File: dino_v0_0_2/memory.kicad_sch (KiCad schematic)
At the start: 15 parts, among them U19 74LS245, U21 74LS245, U24 AT28C256, U26 MCM60256AP, U51 7400, U74 74LS00, U75 74LS32

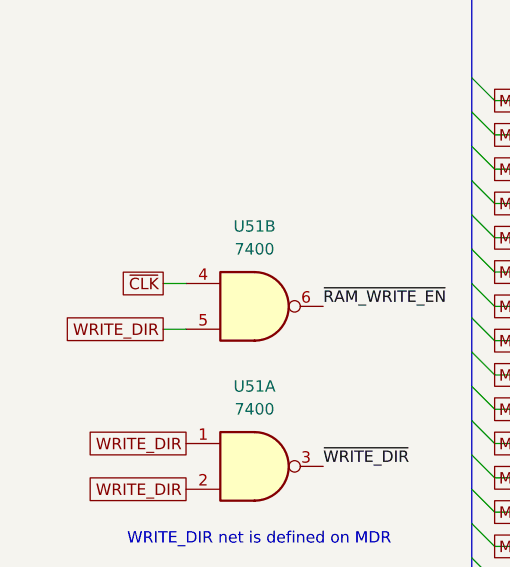
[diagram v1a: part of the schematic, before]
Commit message: fix(copper): gate the RAM write strobe off in T-state 0; RAM-fetch halt closed
A RET fetched from RAM latched 0xFF. Scope work on 2026-09-29 found the
cause: the FETCH row's transparent IR moves the microcode EEPROM address
during CLK-low, the DST decoder (U30.7, code 111 = ~RAM_LOAD) runts for
14-16 ns on some opcode transitions, and NAND(WRITE_DIR, ~CLK) is open
then. The RAM got a 14 ns ~WE at PC's address; the cell survived, the
chip's read output did not, and IR latched 0xFF. From ROM the same runt
is harmless (M15 = 0). The same runt reached ~IO_WR and wrote 0x00 into
[MAR] at every RESET.

Fix: ~RAM_WRITE_EN = NAND(WRITE_DIR, WR_GATE), WR_GATE = NOR(CLK, ~TO0)
on U62 g4, with U56 3->4 inverting TO0 (U7.15). Drawn on control_word
(U62 g4), root (U56 sec 2) and memory (U51.4 label); ERC 0; six pins
beeped good against the drawing.

Witnesses: retlda 40/40 return (was 7/8 halting), no ~WE pulse under
59 ns in 10 runs on a pulse trigger, step2/retmvi/retcrlf/callret/
retinr/retldam/rethlsp 5/5 each, bigxfer returns, a planted byte at
0x8200 survives halt + RESET, and asm/ram/life.asm (Rule 30) runs to the
wall for the first time.

Docs: CLAUDE.md rewritten present-tense (facts only); every retraction
moved to .git/sdd/MISTAKES_MISSTEPS.md. test_ramret.py's table is marked
as the pre-gate record. RAM image headers stamped with the post-gate
result. dino_sheet_contracts.md regenerated by kicad_contracts.py.

Co-Authored-By: Claude Fable 5.1 <noreply@anthropic.com>
Claude-Session: https://claude.ai/code/session_01JGxSS4MVUcaZdKZGtKroSg
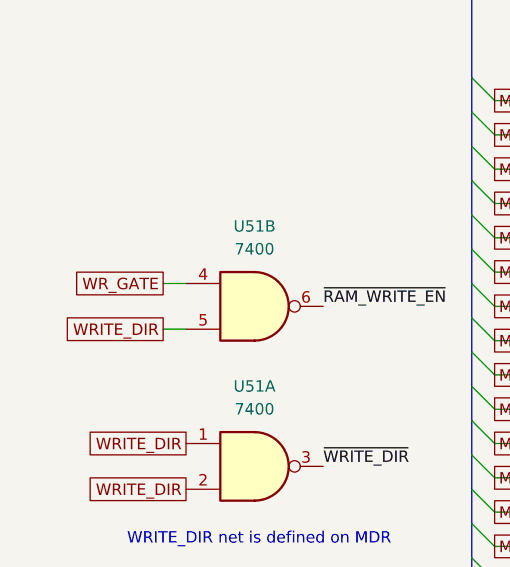
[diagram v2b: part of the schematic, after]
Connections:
- net ~{CLK} renamed WR_GATE
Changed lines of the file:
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@@
 		)
 	)
-	(global_label "~{CLK}"
+	(global_label "WR_GATE"
 		(shape passive)
 		(at 26.67 63.5 180)

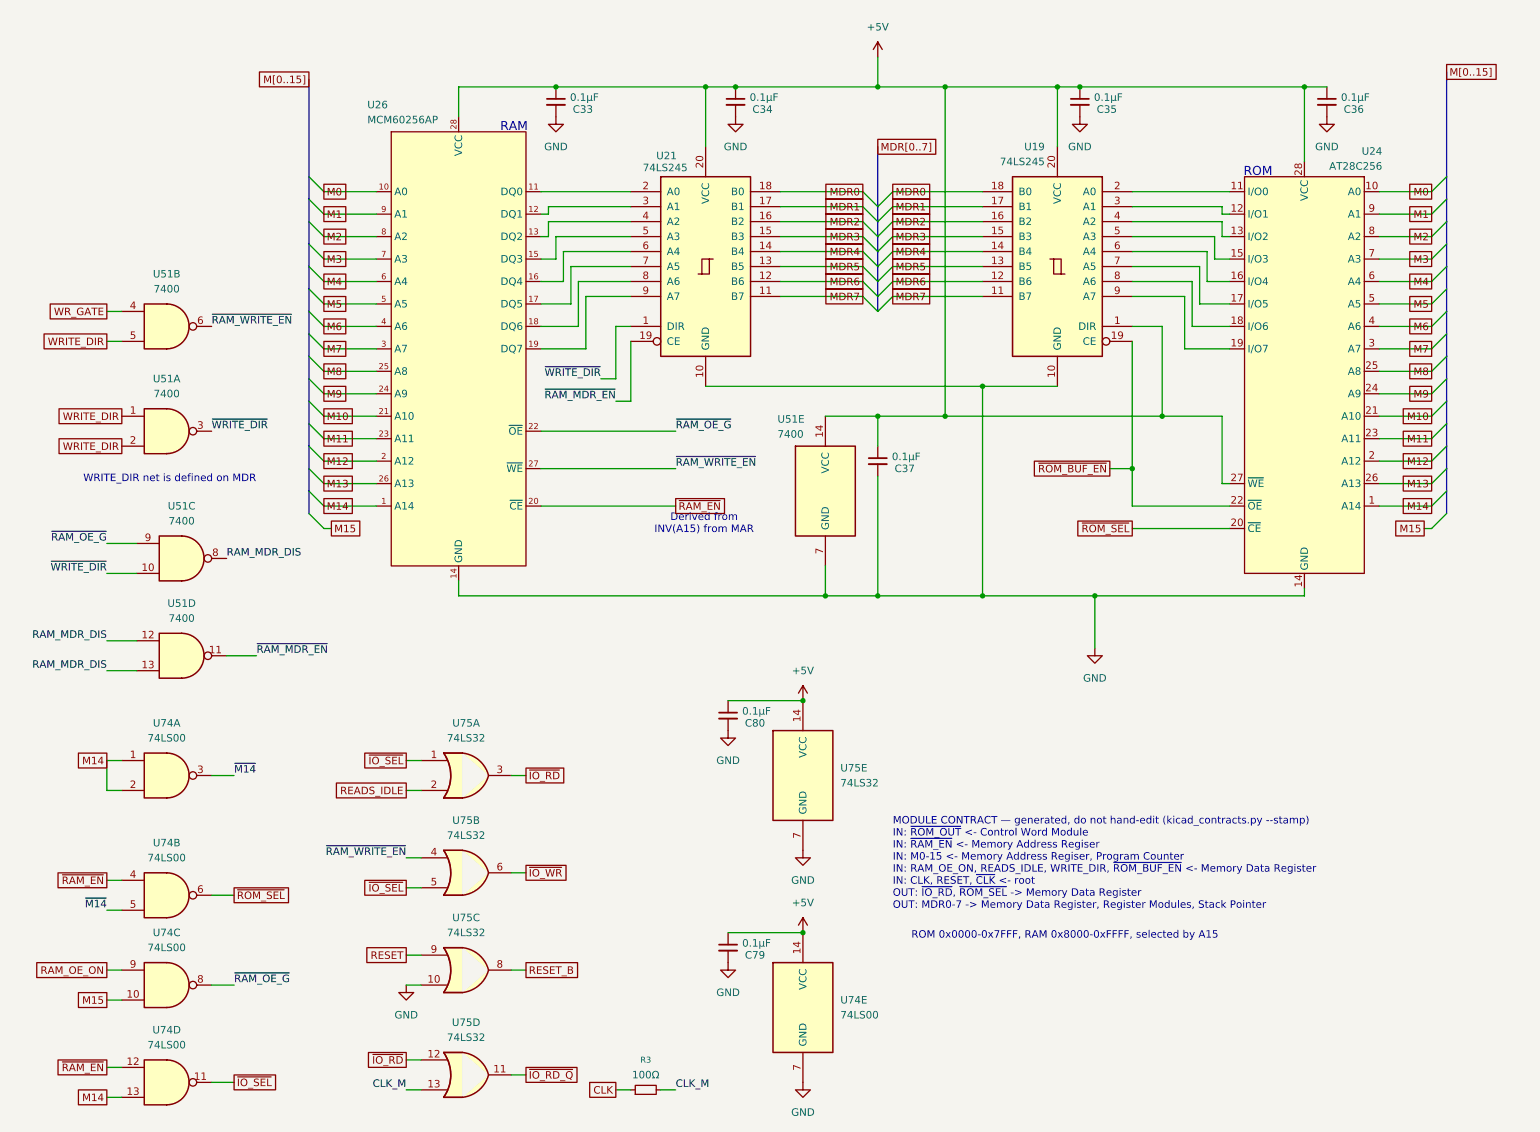
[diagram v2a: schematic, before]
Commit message: feat(int): draw the interrupt block; sheet cleanup pass
New sheet dino_v0_0_2/interrupt.kicad_sch (page 15): U80-U87, R28 4.7k
pull-up on ~{IRQ}, R29 100R on the block's CLK branch, C83-C90. Every
pin per PHASE_INT SECTION 3, checked against the plan with kicad_netlist
and kicad-cli (146 pins, 0 mismatches).

Old sheets (SECTION 3.2): U28.4 lifted off GND to INJECT; U61.3 to
END_OR_ACCEPT; U36.1 to PC_UP_GATED; U49 D0-3 cut from U48 Za-Zd and
routed through U87 as FLAG_NEXT0-3 / FLAG_D0-3; FLAG_C/Z/V/N and the
five decoder outputs made global. dino_serial: U104 74LS05, INTR ->
~{IRQ}, C4.

Placement pass on every sheet: bus entries and global labels no longer
share wires; M, CW, T, IRB and SA buses kept as labelled keys. Nets
diffed against HEAD per sheet: only the intended changes and a rotated
C29. Project ERC: 0 errors. MODULE CONTRACT stamps regenerated.

Co-Authored-By: Claude Fable 5.1 <noreply@anthropic.com>
Claude-Session: https://claude.ai/code/session_01JGxSS4MVUcaZdKZGtKroSg
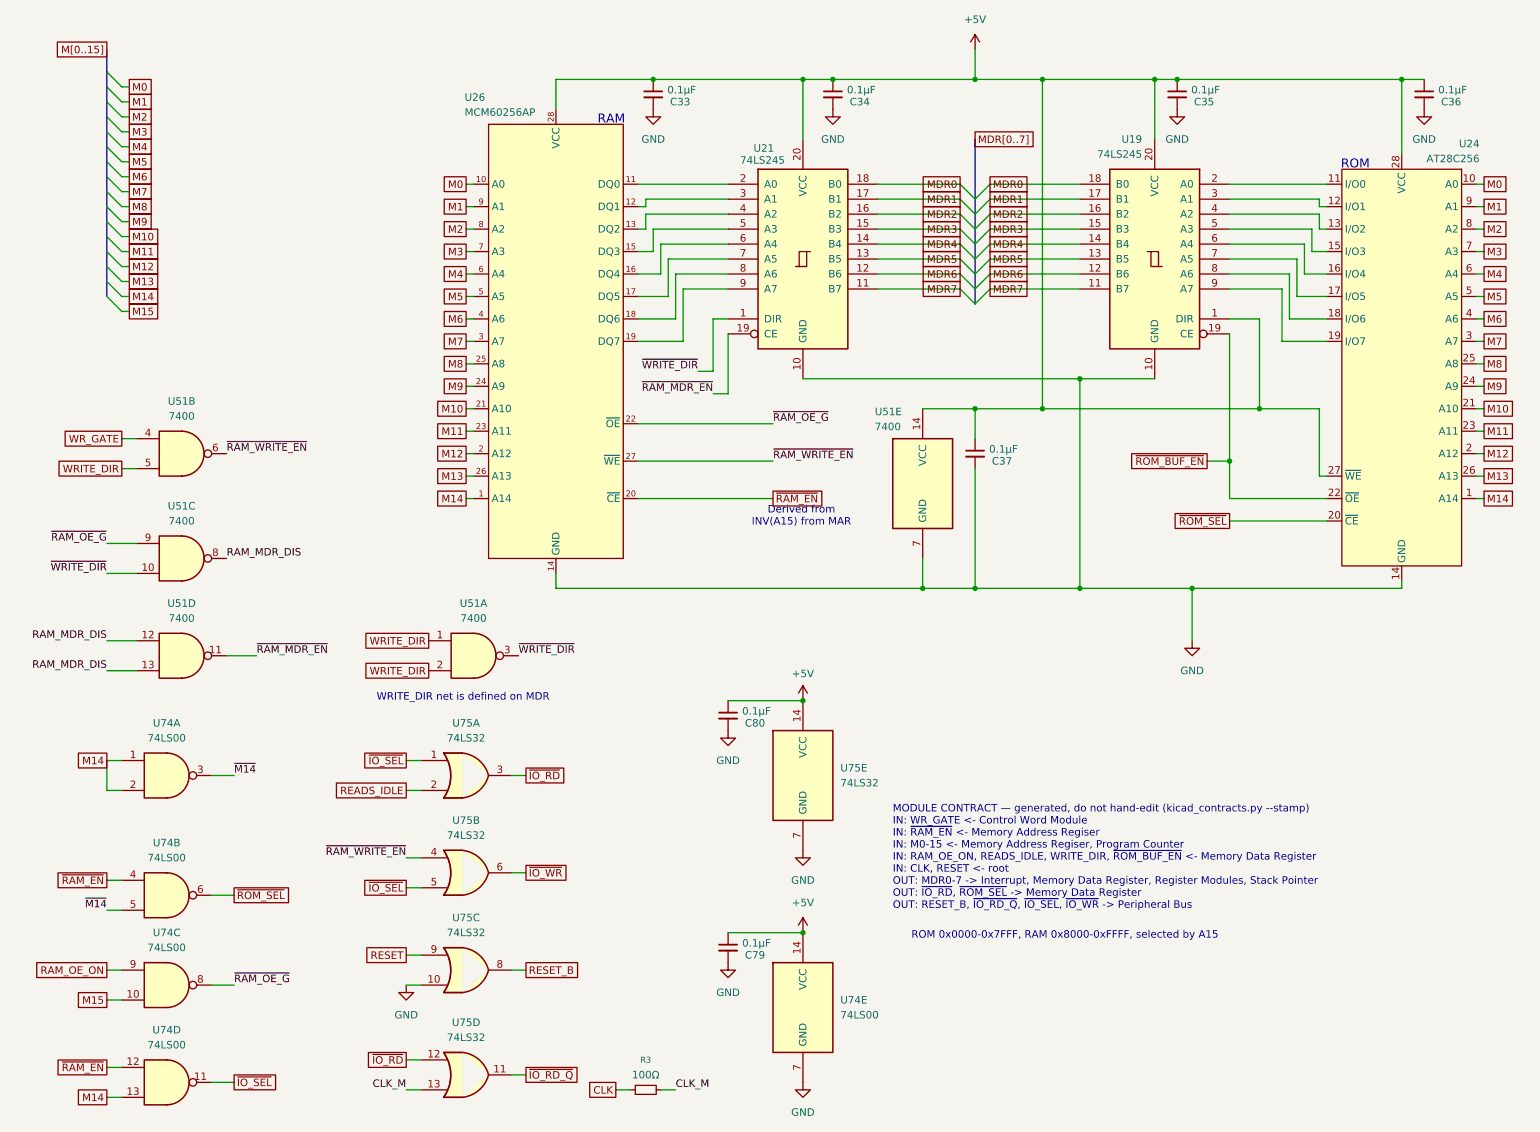
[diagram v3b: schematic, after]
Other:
- note added: "MODULE CONTRACT — generated, do not hand-edit (kicad_contracts.py --stamp) IN: WR_GATE <- Control Word Module IN: ~{RAM_EN} <- Memory Address Regiser IN: M0-15 <- Memory Address Regiser, Program Counter IN: RAM_OE_ON, READS_IDLE, WRITE_DIR, ~{ROM_BUF_EN} <- Memory Data Register IN: CLK, RESET <- root OUT: MDR0-7 -> Interrupt, Memory Data Register, Register Modules, Stack Pointer OUT: ~{IO_RD}, ~{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"
- note removed: "MODULE CONTRACT — generated, do not hand-edit (kicad_contracts.py --stamp) IN: ~{ROM_OUT} <- Control Word Module IN: ~{RAM_EN} <- Memory Address Regiser IN: M0-15 <- Memory Address Regiser, Program Counter IN: RAM_OE_ON, READS_IDLE, WRITE_DIR, ~{ROM_BUF_EN} <- Memory Data Register IN: CLK, RESET, ~{CLK} <- root OUT: ~{IO_RD}, ~{ROM_SEL} -> Memory Data Register OUT: MDR0-7 -> Memory Data Register,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"
- moved on the sheet: C33, C34, C35, C36, C37, U19, U21, U24, U26, U51A, U51B, U51E

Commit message: feat(pcb): Rev 1.0 pre-order batch, debug access, no fuse
From the five-way pre-order review:

- Debug: J14 clock select at U27.3 (1.024 MHz / 512k / 256k / 128k /
  STEP), STEP debounced from SW3 through the spare U56 5->6 Schmitt;
  J15 LA header (16 control signals, a GND beside each); J16 power for
  the OB LEDs; DNP cap pads C94/C95/C96 on CLK at U6.2, CLK_ALU at
  U47.11 and CW15 (HALT) at U61.5; 15 GND scope loops so every IC but
  two is within 50 mm of one, plus a +5V test point.
- Power: F1 removed, no fuse (Rico); J9's +5V solid to the plane;
  bulk C97-C100 100 uF spread across the board; C92 ceramic.
- Layout: U6 beside U27 (its CLK pin was 138 mm out on raw CLK), C1/R1
  beside U56, RST_SIG in RESET and CLK_R / CLK_INT / CLK_M / CLK_SEL in
  CLK, thermal gap 0.3 mm (GND plane slots from 25 mm to under 8 mm),
  tracks >= 0.2 mm with no neckdown (6/6 mil tier), board min track rule.
- Values to match the bench: U56 SN7414N, U36 74LS00, U51 DM7400N,
  Y1 4.096 MHz.
- Edge socket: silk outline and a pin-1 arrow (unkeyed; a reversed card
  shorts +5V).

Re-routed by Freerouting 2.5.0 from an empty board. KiCad DRC 0
unconnected / 0 errors, schematic parity 0, one text_thickness warning
on the TrueType board text; ERC at its 74 baseline; test_pcb_envelope
7/7. Clock copper: CLK 296 mm, ~{CLK} 283, CLK_B 162, CLK_ALU 48.
Fab: fabrication/dino_rev_1_0_gerbers_20261029_1153.zip.

Co-Authored-By: Claude Opus 5.5 <noreply@anthropic.com>
Claude-Session: https://claude.ai/code/session_01JGxSS4MVUcaZdKZGtKroSg
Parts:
- U51: value 7400 -> DM7400N
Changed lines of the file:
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@@
 			)
 		)
-		(property "Value" "7400"
+		(property "Value" "DM7400N"
 			(at 39.3617 115.57 0)
 			(show_name no)
@@
 			)
 		)
-		(property "Value" "7400"
+		(property "Value" "DM7400N"
 			(at 39.3617 99.06 0)
 			(show_name no)
@@
 			)
 		)
-		(property "Value" "7400"
+		(property "Value" "DM7400N"
 			(at 156.972 83.058 0)
 			(show_name no)
@@
 			)
 		)
-		(property "Value" "7400"
+		(property "Value" "DM7400N"
 			(at 88.8917 115.57 0)
 			(show_name no)
@@
 			)
 		)
-		(property "Value" "7400"
+		(property "Value" "DM7400N"
 			(at 39.3617 81.28 0)
 			(show_name no)
